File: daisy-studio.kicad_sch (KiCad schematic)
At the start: 5 parts

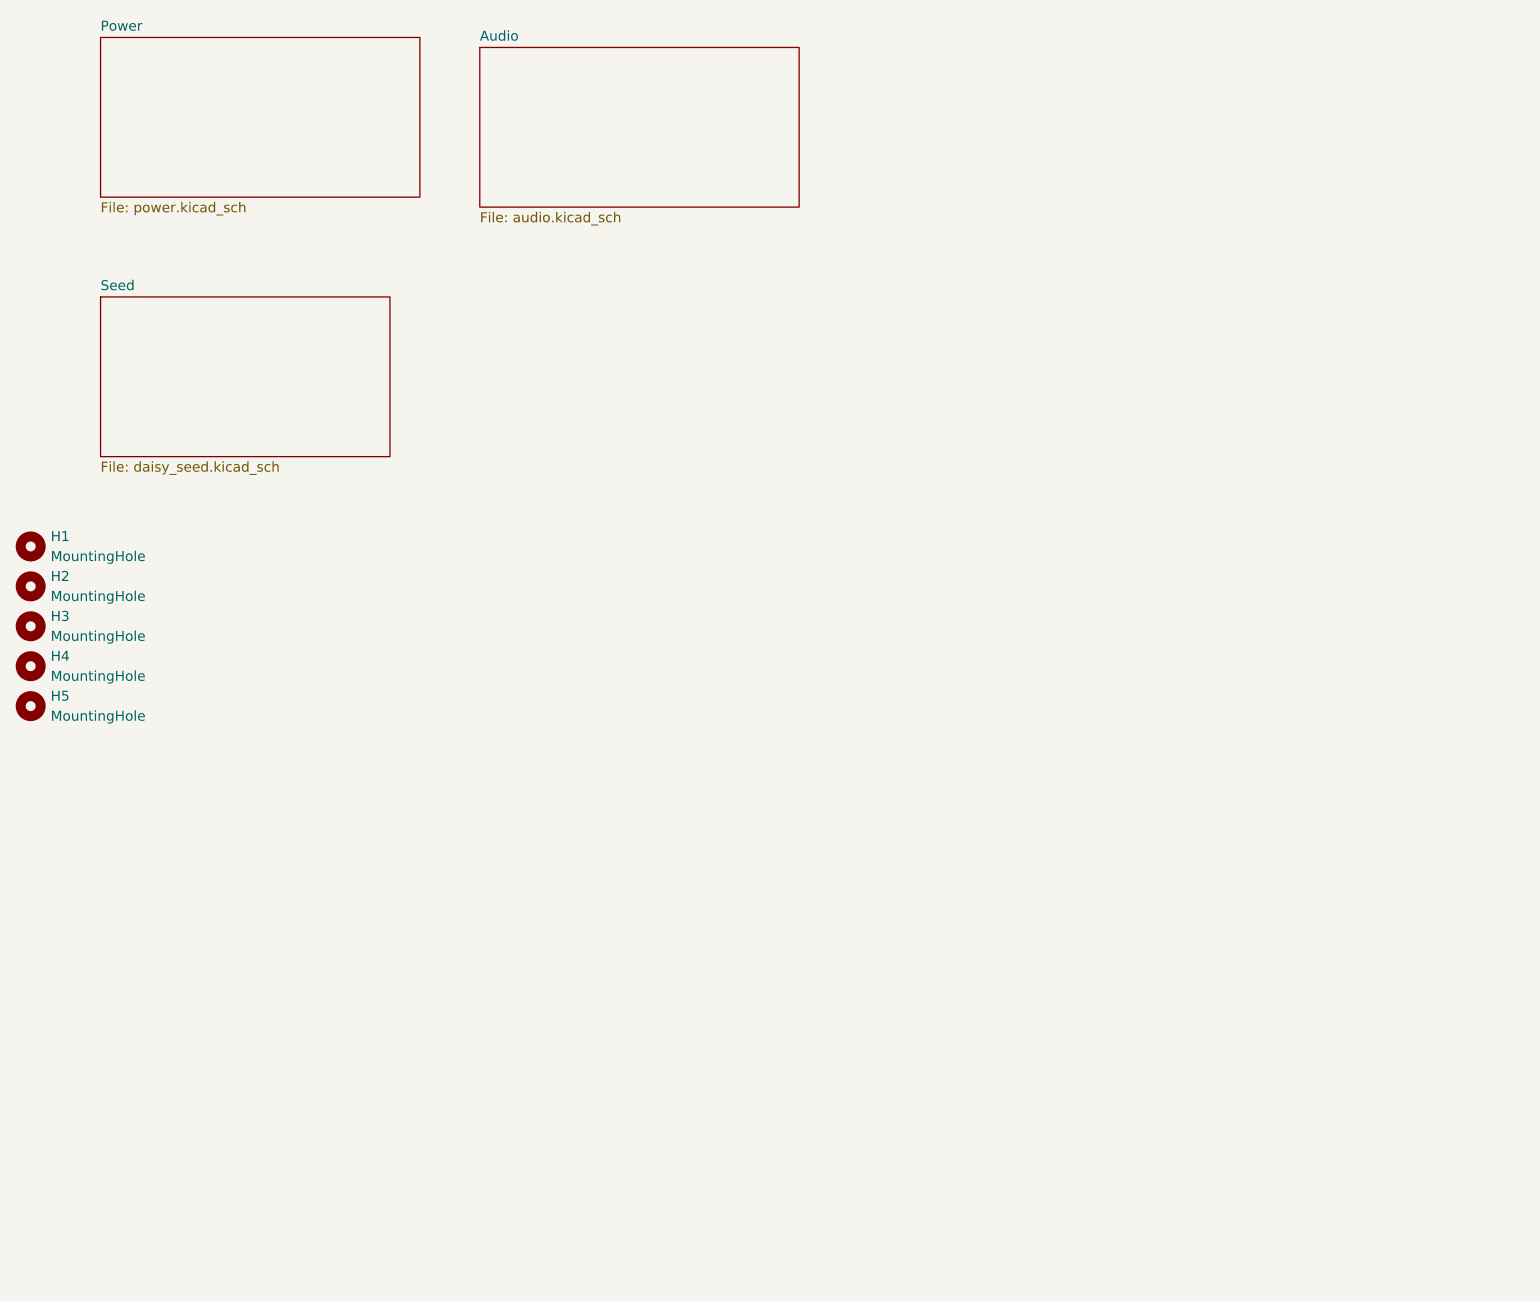
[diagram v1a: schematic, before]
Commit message: audio input for rev 2 laid out in schematic
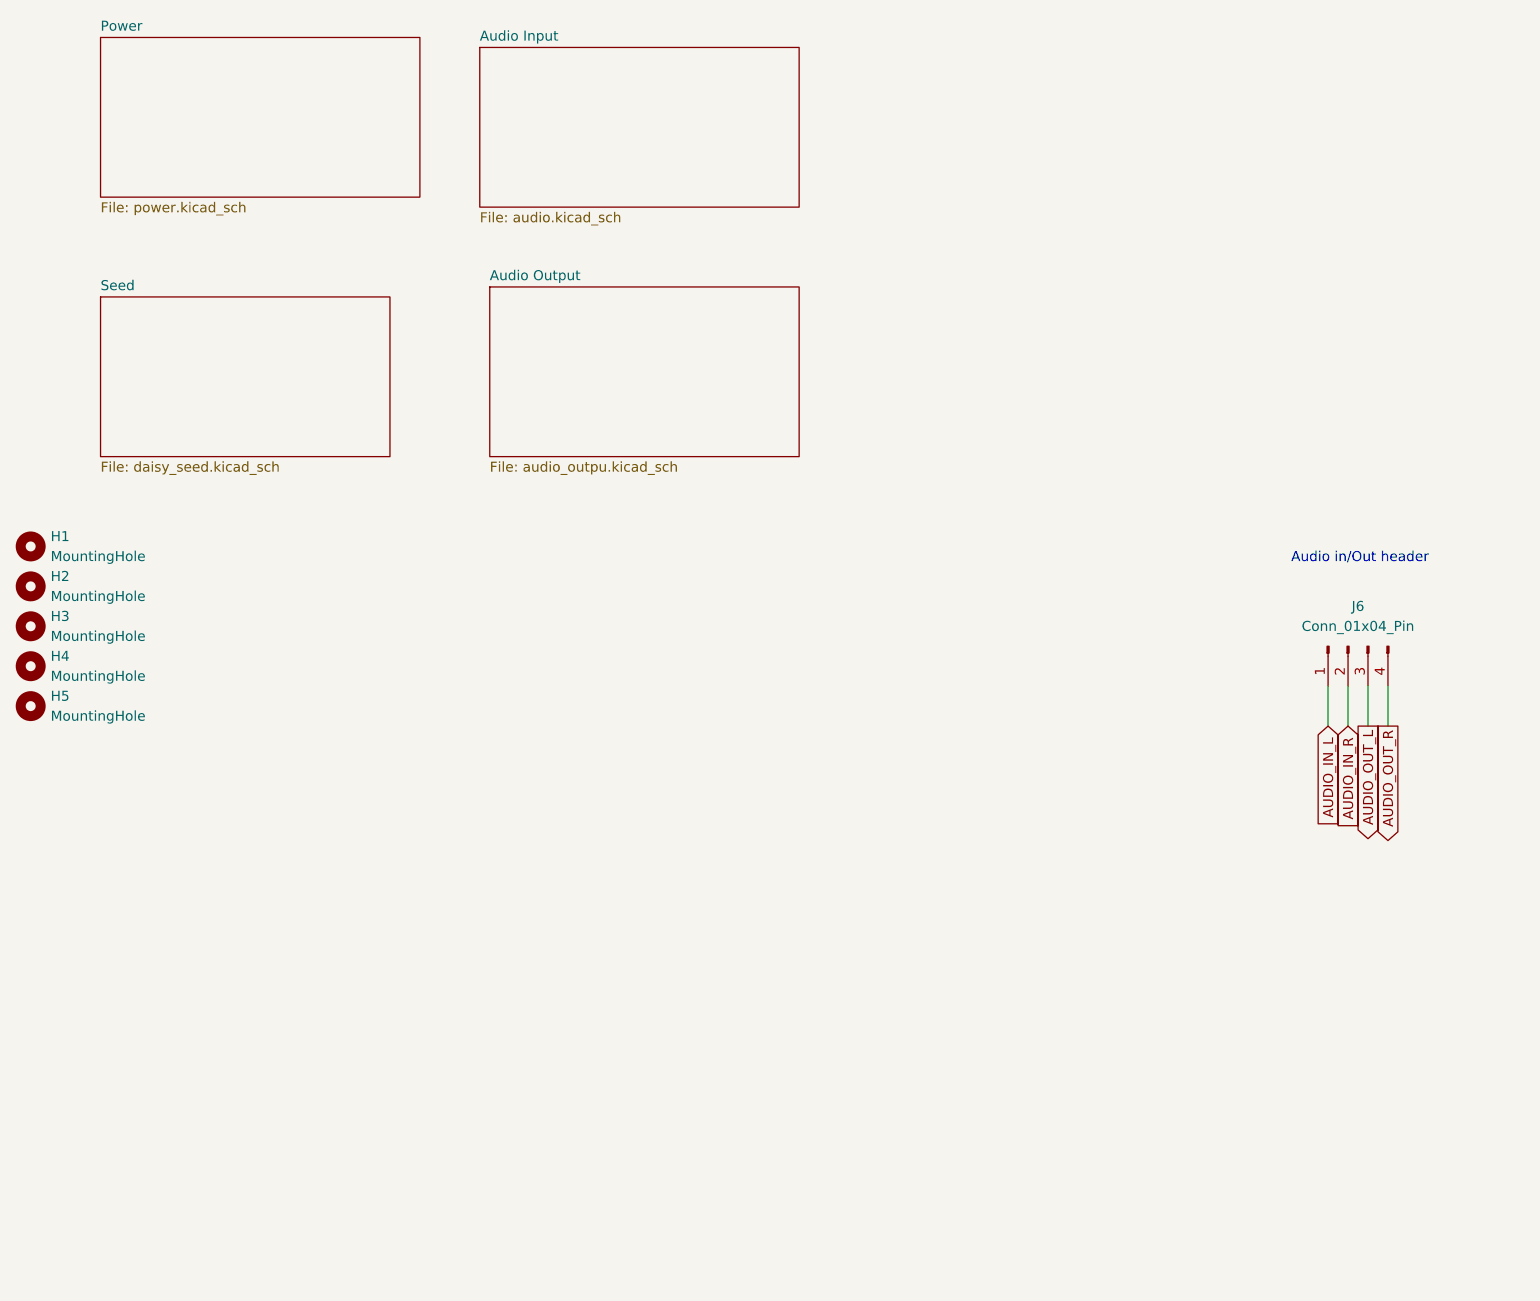
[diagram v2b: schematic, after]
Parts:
- added J6: Conn_01x04_Pin, Connector_PinHeader_2.54mm:PinHeader_1x04_P2.54mm_Vertical, symbol Connector:Conn_01x04_Pin
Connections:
- new net AUDIO_IN_L: J6.1 (Pin_1)
- new net AUDIO_IN_R: J6.2 (Pin_2)
- new net AUDIO_OUT_L: J6.3 (Pin_3)
- new net AUDIO_OUT_R: J6.4 (Pin_4)
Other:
- sheet Audio renamed Audio Input
- added sheet Audio Output (audio_outpu.kicad_sch)
- note added: "Audio in/Out header"
- title: Triptech Carrier Board -> Daisy-Studio

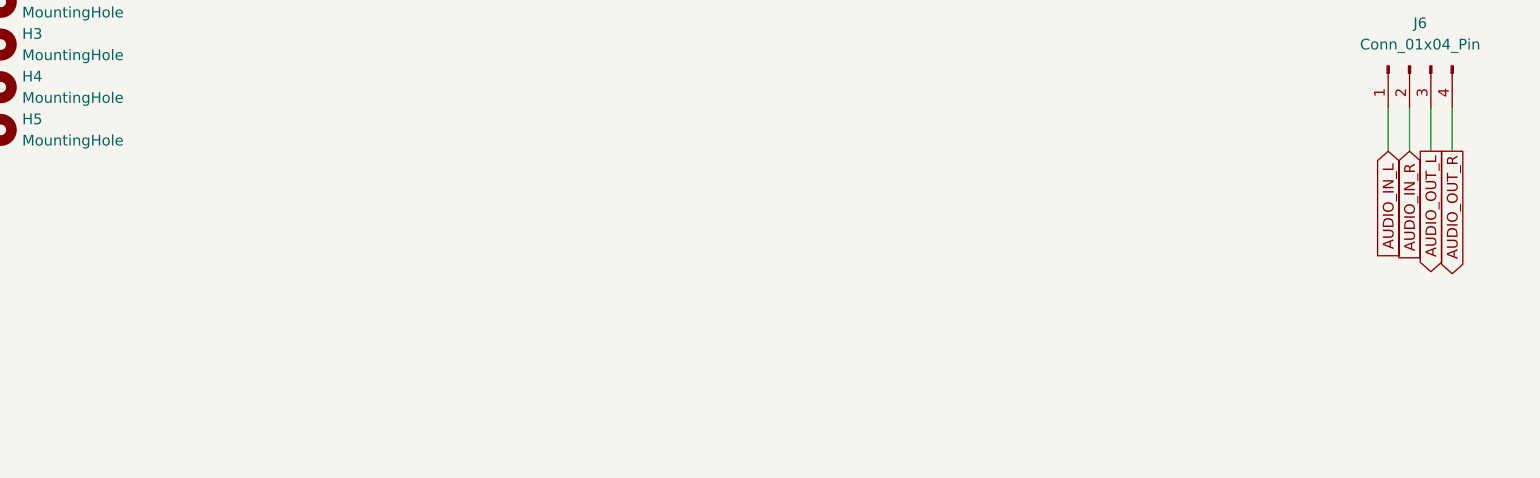
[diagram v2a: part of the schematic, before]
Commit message: Cleanup and review of input pt 1
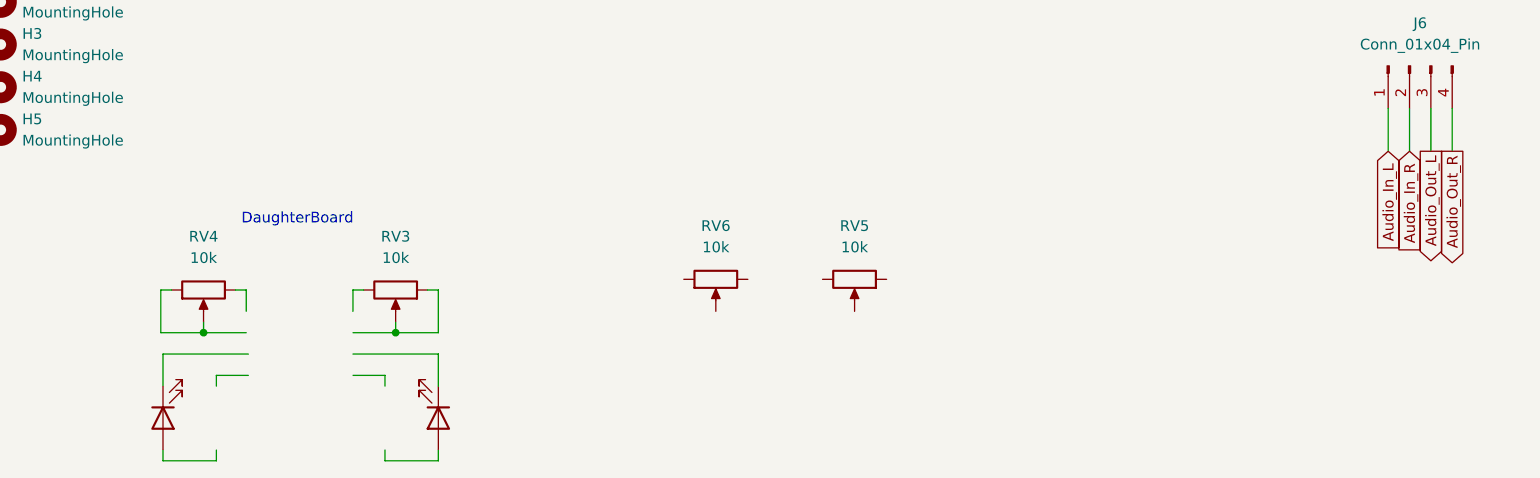
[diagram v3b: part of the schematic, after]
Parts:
- added D2, D4: LED, symbol Device:LED
- added RV3, RV4, RV5, RV6: 10k, symbol Device:R_Potentiometer
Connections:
- net AUDIO_IN_L renamed Audio_In_L
- net AUDIO_IN_R renamed Audio_In_R
- net AUDIO_OUT_L renamed Audio_Out_L
- net AUDIO_OUT_R renamed Audio_Out_R
- new net: RV3.1, RV3.2
- new net: RV4.1, RV4.2
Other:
- note added: "DaughterBoard"

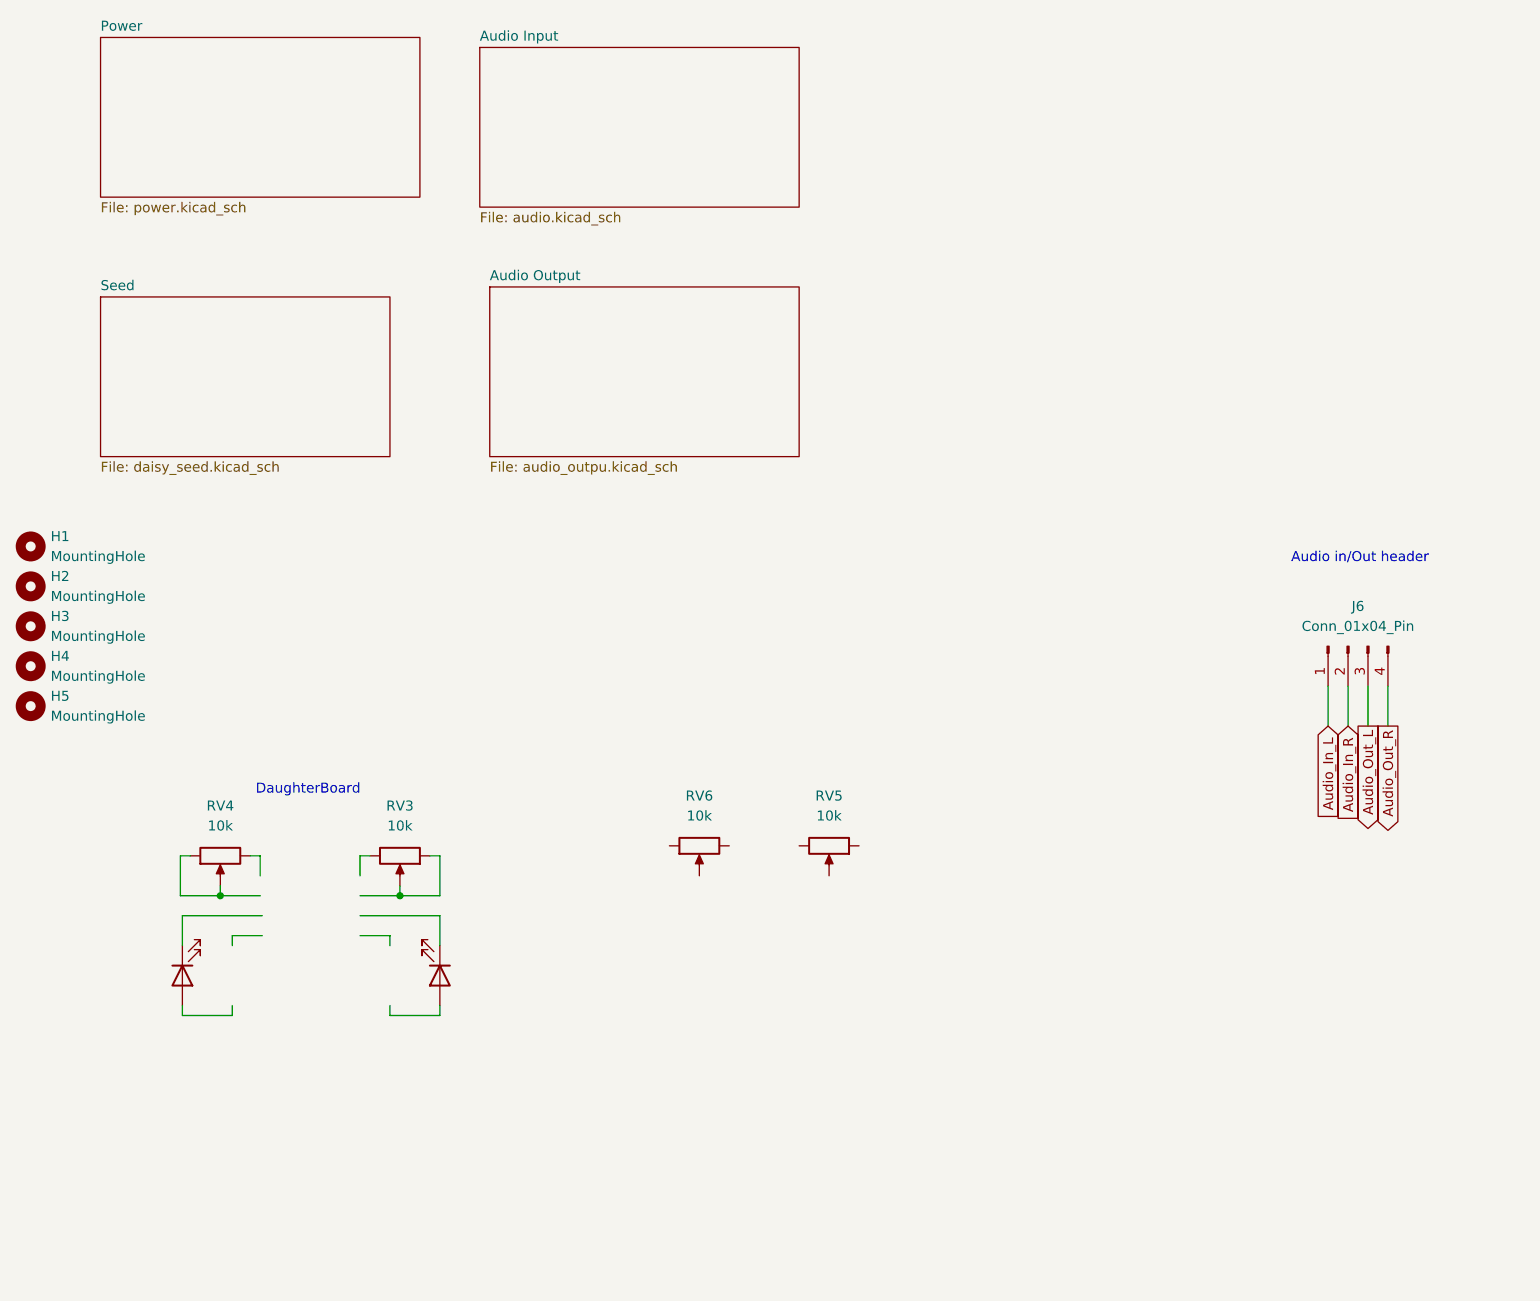
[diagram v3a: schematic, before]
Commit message: fix some footprints
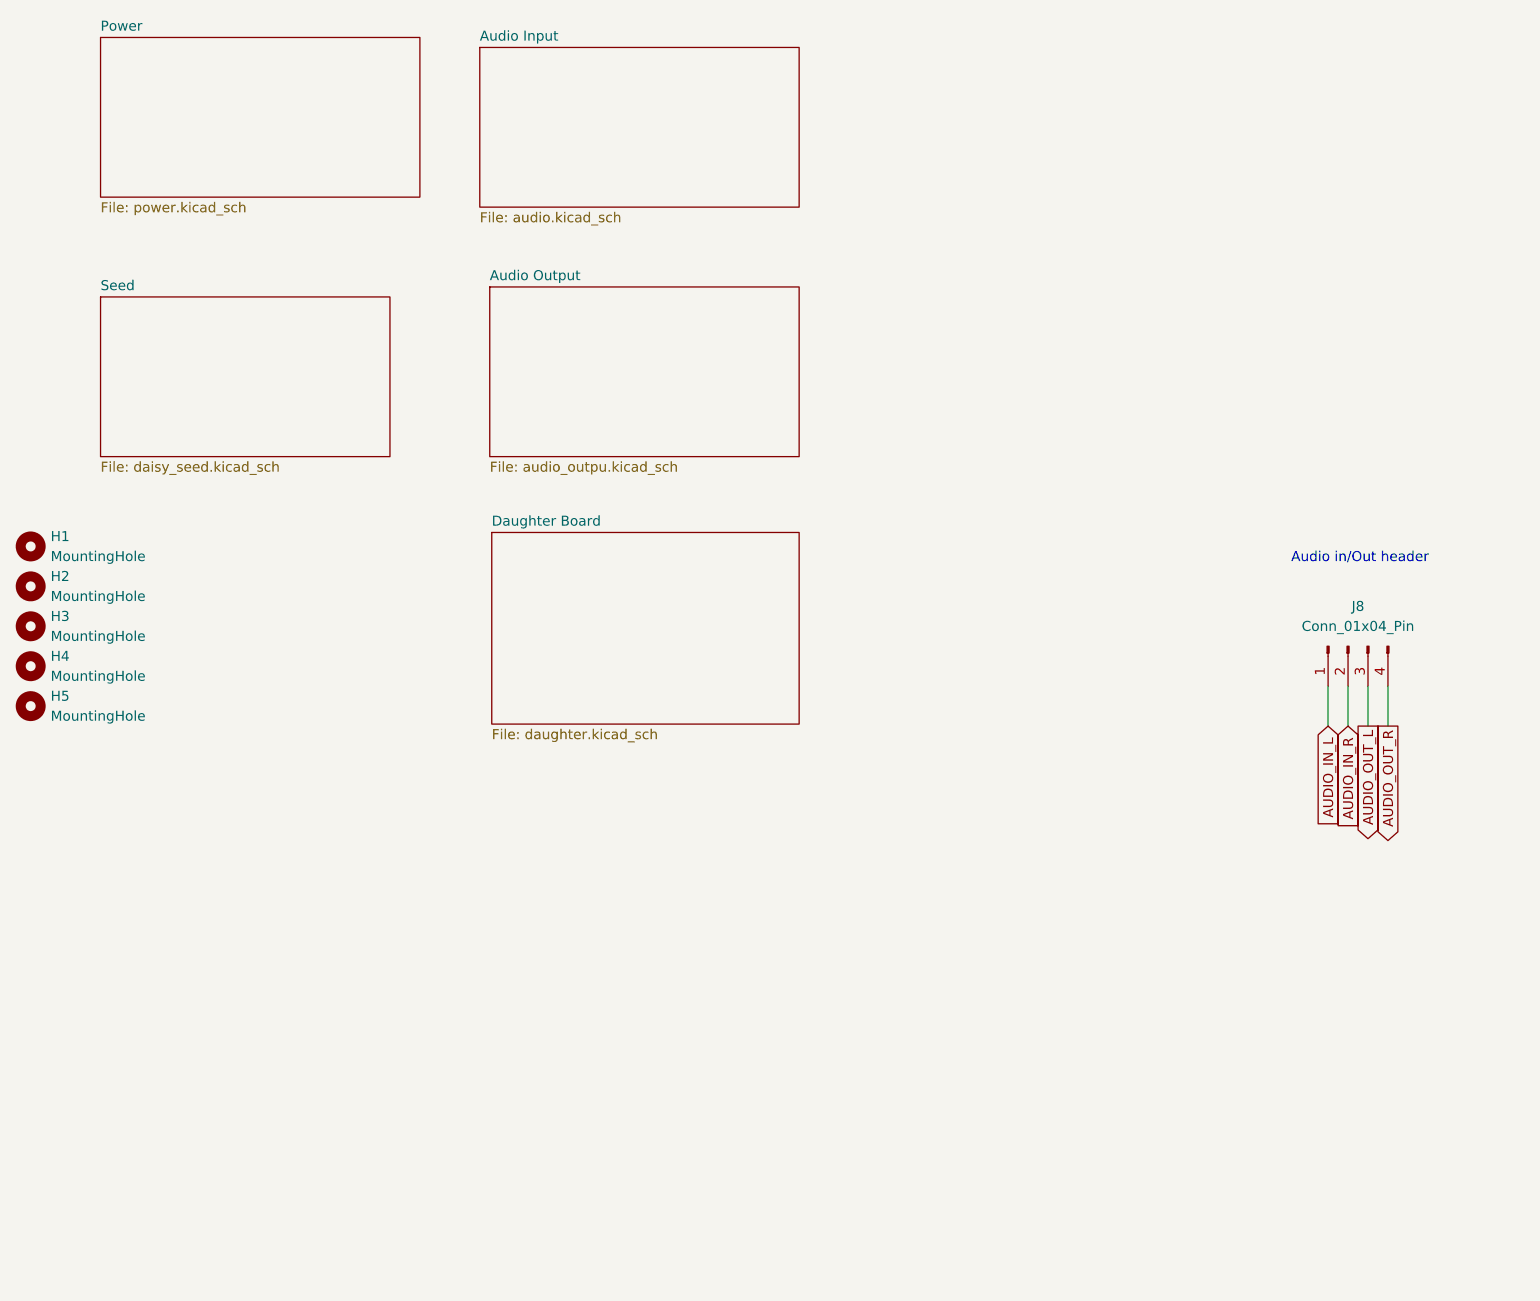
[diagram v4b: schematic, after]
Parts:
- removed D2, D4: LED, symbol Device:LED
- removed RV3, RV4, RV5, RV6: 10k, symbol Device:R_Potentiometer
- renumbered J6 to J8
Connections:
- net Audio_In_L renamed AUDIO_IN_L
- net Audio_In_R renamed AUDIO_IN_R
- net Audio_Out_L renamed AUDIO_OUT_L
- net Audio_Out_R renamed AUDIO_OUT_R
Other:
- added sheet Daughter Board (daughter.kicad_sch)
- note removed: "DaughterBoard"
